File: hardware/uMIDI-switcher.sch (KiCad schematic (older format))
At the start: 26 parts, among them U1 MC7809CD, U2 MC7809CD, U3 MC7809CD, U4 MC7809CD, X1 CONN_01X02, X14 uMIDI GPIO, X16 uMIDI Power, X2 CONN_01X02, X3 CONN_01X02, X4 CONN_01X02, X5 Jack_Stacked, X6 Jack_Stacked

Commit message: Re-Annotate
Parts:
- renumbered C9 to C10, C28 to C12, C10 to C8, C8 to C9, X14 to X6, X16 to X7, X6 to X8
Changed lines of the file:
@@
 $EndComp
 $Comp
-L C C9
+L C C10
 U 1 1 55B6FB17
 P 5900 5300
-F 0 "C9" H 5950 5400 50  0000 L CNN
+F 0 "C10" H 5950 5400 50  0000 L CNN
 F 1 "100n" H 5950 5200 50  0000 L CNN
 F 2 "Capacitors_SMD:C_0603" H 5938 5150 30  0001 C CNN
@@
 $EndComp
 $Comp
-L C C8
+L C C9
 U 1 1 55B708C3
 P 4900 5300
-F 0 "C8" H 4950 5400 50  0000 L CNN
+F 0 "C9" H 4950 5400 50  0000 L CNN
 F 1 "100n" H 4950 5200 50  0000 L CNN
 F 2 "Capacitors_SMD:C_0603" H 4938 5150 30  0001 C CNN
@@
 	3850 5500 3850 5450
 $Comp
-L CONN_01X10 X14
+L CONN_01X10 X6
 U 1 1 55FDA32A
 P 4350 1950
-F 0 "X14" H 4350 2500 50  0000 C CNN
+F 0 "X6" H 4350 2500 50  0000 C CNN
 F 1 "uMIDI GPIO" V 4450 1950 50  0000 C CNN
 F 2 "Connect:VASCH5x2" H 4350 1950 60  0001 C CNN
@@
 $EndComp
 $Comp
-L CONN_01X02 X16
+L CONN_01X02 X7
 U 1 1 55FDF236
 P 7550 5250
-F 0 "X16" H 7550 5400 50  0000 C CNN
+F 0 "X7" H 7550 5400 50  0000 C CNN
 F 1 "uMIDI Power" V 7650 5250 50  0000 C CNN
 F 2 "Connect:PINHEAD1-2" H 7550 5250 60  0001 C CNN
@@
 	7350 5050 7350 5200
 $Comp
-L C C28
+L C C12
 U 1 1 55FDFE71
 P 7100 5300
-F 0 "C28" H 6900 5400 50  0000 L CNN
+F 0 "C12" H 6900 5400 50  0000 L CNN
 F 1 "100n" H 6850 5200 50  0000 L CNN
 F 2 "Capacitors_SMD:C_0603" H 7138 5150 30  0001 C CNN
@@
 	7350 5500 7350 5300
 $Comp
-L C C10
+L C C8
 U 1 1 55FECDD5
 P 4550 5300
-F 0 "C10" H 4600 5400 50  0000 L CNN
+F 0 "C8" H 4600 5400 50  0000 L CNN
 F 1 "10u" H 4600 5200 50  0000 L CNN
 F 2 "Capacitors_SMD:C_1206" H 4588 5150 30  0001 C CNN
@@
 Connection ~ 1550 2000
 $Comp
-L Jack_Stacked X6
+L Jack_Stacked X8
 U 1 1 56223ACE
 P 8300 2650
-F 0 "X6" H 7450 4650 60  0000 C CNN
+F 0 "X8" H 7450 4650 60  0000 C CNN
 F 1 "Jack_Stacked" H 7400 2900 60  0000 C CNN
 F 2 "uMIDI-switcher:NSJ12HF-1" H 8300 2650 60  0001 C CNN

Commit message: Change LDO supplier
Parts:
- U1, U2, U3, U4: Manufacturer (none) -> ON Semiconductor; Manufacturer Part Number (none) -> MC7809CD2TG; Part Number MC7809CD2TGOS-ND -> 863-MC7809CD2TG; Supplier Digikey -> Mouser
- X5, X8: Manufacturer (none) -> Neutrik; Manufacturer Part Number (none) -> NSJ12HF-1

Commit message: Add some component fields; Change 10uF footprint
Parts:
- C1, C10, C12, C2, C3, C4, C5, C6, C9: Manufacturer (none) -> Murata; Manufacturer Part Number (none) -> GRM188R71E104KA01D; Supplier Link (none) -> http://eu.mouser.com/ProductDetail/Murata-Electronics/GRM18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; Supplier Part Number (none) -> 81-GRM39X104K25
- C11, C7, C8: footprint Capacitors_SMD:C_1206 -> Capacitors_SMD:C_0805; Manufacturer (none) -> Murata; Manufacturer Link (none) -> http://psearch.en.murata.com/capacitor/lineup/grm/; Manufacturer Part Number (none) -> GRM21BR61E106KA73L; Supplier Link (none) -> http://eu.mouser.com/ProductDetail/Murata-Electronics/GRM21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; Supplier Part Number (none) -> 81-GRM21BR61E106KA3L
- D1: Part Number 621-B160-F -> (none); Supplier Link (none) -> http://eu.mouser.com/ProductDetail/Diodes-Incorporated/B160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; Supplier Part Number (none) -> 621-B160-F
- R1: Manufacturer (none) -> Vishay/Dale; Manufacturer Link (none) -> http://www.vishay.com/resistors-fixed/list/product-20011/; Manufacturer Part Number (none) -> CRCW0603100MJPEAHR; Supplier Link (none) -> http://eu.mouser.com/ProductDetail/Vishay-Dale/CRCW0603100M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; Supplier Part Number (none) -> 71-CRCW0603100MJPEA
- U1, U2, U3, U4: Part Number 863-MC7809CD2TG -> (none); Supplier Link (none) -> http://eu.mouser.com/ProductDetail/ON-Semiconductor/MC7809C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; Supplier Part Number (none) -> 863-MC7809CD2TG
- X5, X8: Part Number 568-NSJ12HF-1 -> (none); Supplier Link (none) -> http://www.mouser.de/ProductDetail/Neutrik/NSJ12HF-1/?qs=%2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; Supplier Part Number (none) -> 568-NSJ12HF-1
- X6: Manufacturer (none) -> 3M Electronic Solutions Division; Manufacturer Link (none) -> 30310-6002HB; Supplier Link (none) -> http://eu.mouser.com/ProductDetail/3M-Electronic-Solutions-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; Supplier Part Number (none) -> 517-30310-6002

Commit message: Fix ribbon connector supplier fields
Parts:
- X6: Manufacturer Link 30310-6002HB -> (none); Manufacturer Part Number (none) -> 30310-6002HB
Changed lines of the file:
@@
 F 6 "http://eu.mouser.com/ProductDetail/3M-Electronic-Solutions-Division/30310-6002HB/?qs=sGAEpiMZZMs%252bGHln7q6pmwu5ra4CY41iHF1AQhwXwqM%3d" H 4350 2500 60  0001 C CNN "Supplier Link"
 F 7 "3M Electronic Solutions Division" H 4350 2500 60  0001 C CNN "Manufacturer"
-F 8 "" H 4350 2500 60  0001 C CNN "Manufacturer Part Number"
-F 9 "30310-6002HB" H 4350 2500 60  0001 C CNN "Manufacturer Link"
+F 8 "30310-6002HB" H 4350 2500 60  0001 C CNN "Manufacturer Part Number"
 	1    4350 1950
 	-1   0    0    -1

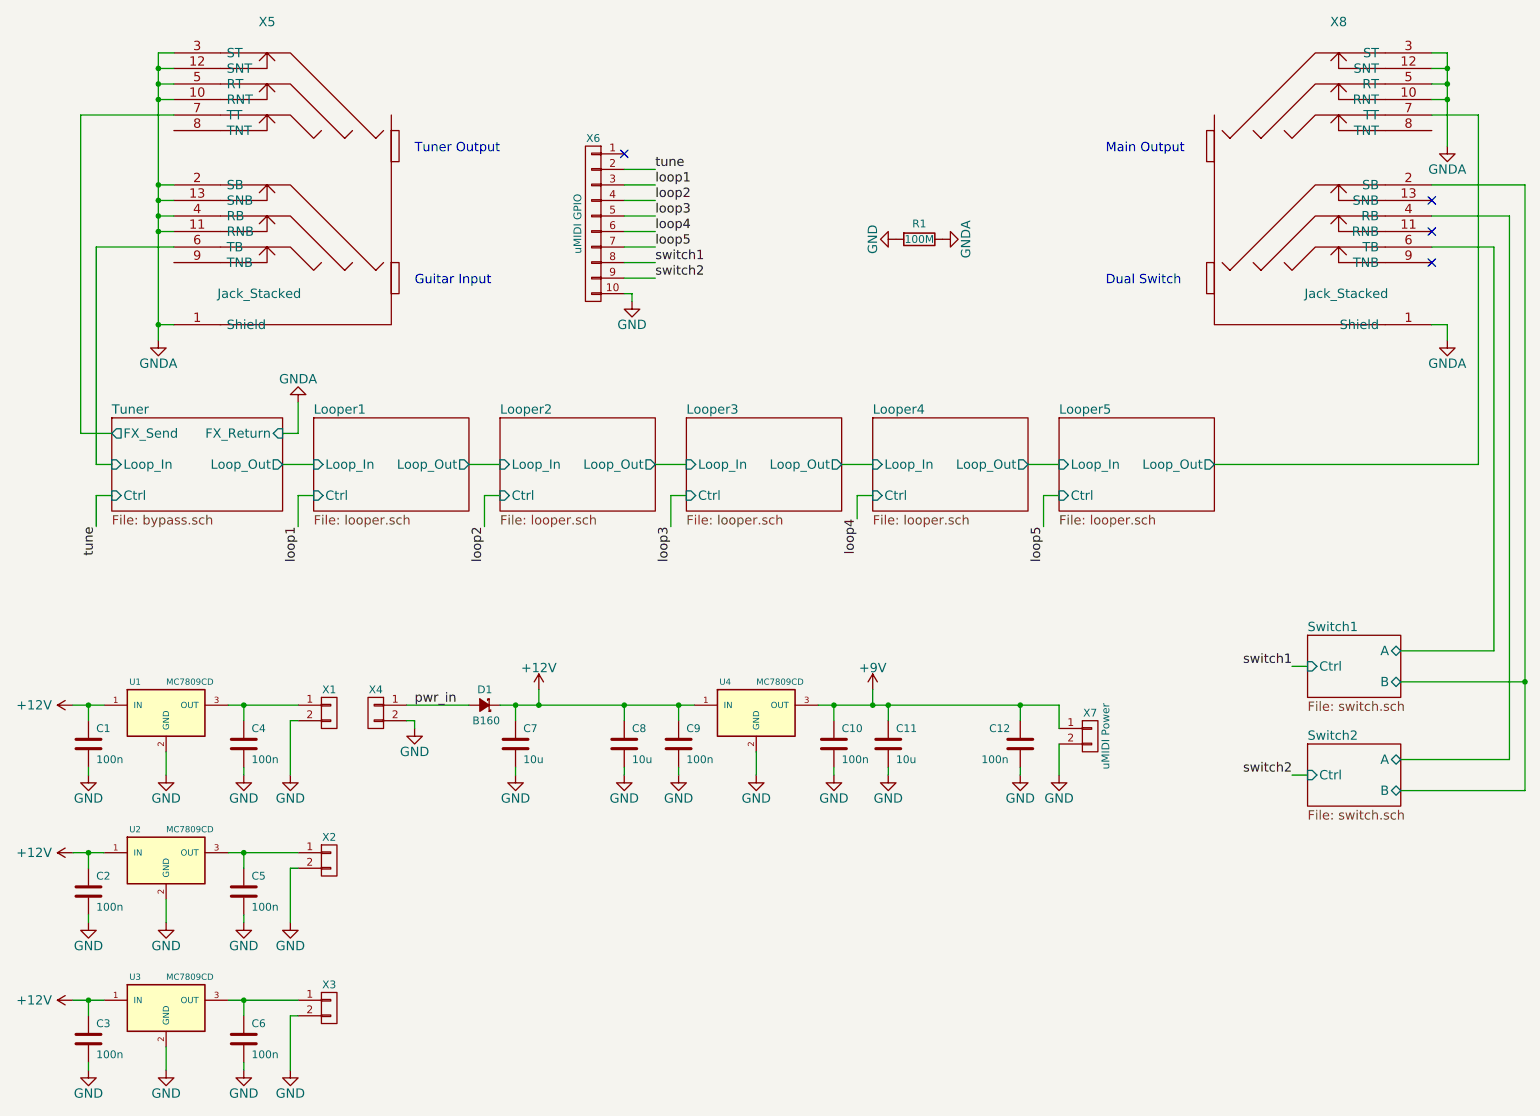
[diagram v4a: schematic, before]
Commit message: Straighten annotation and placement
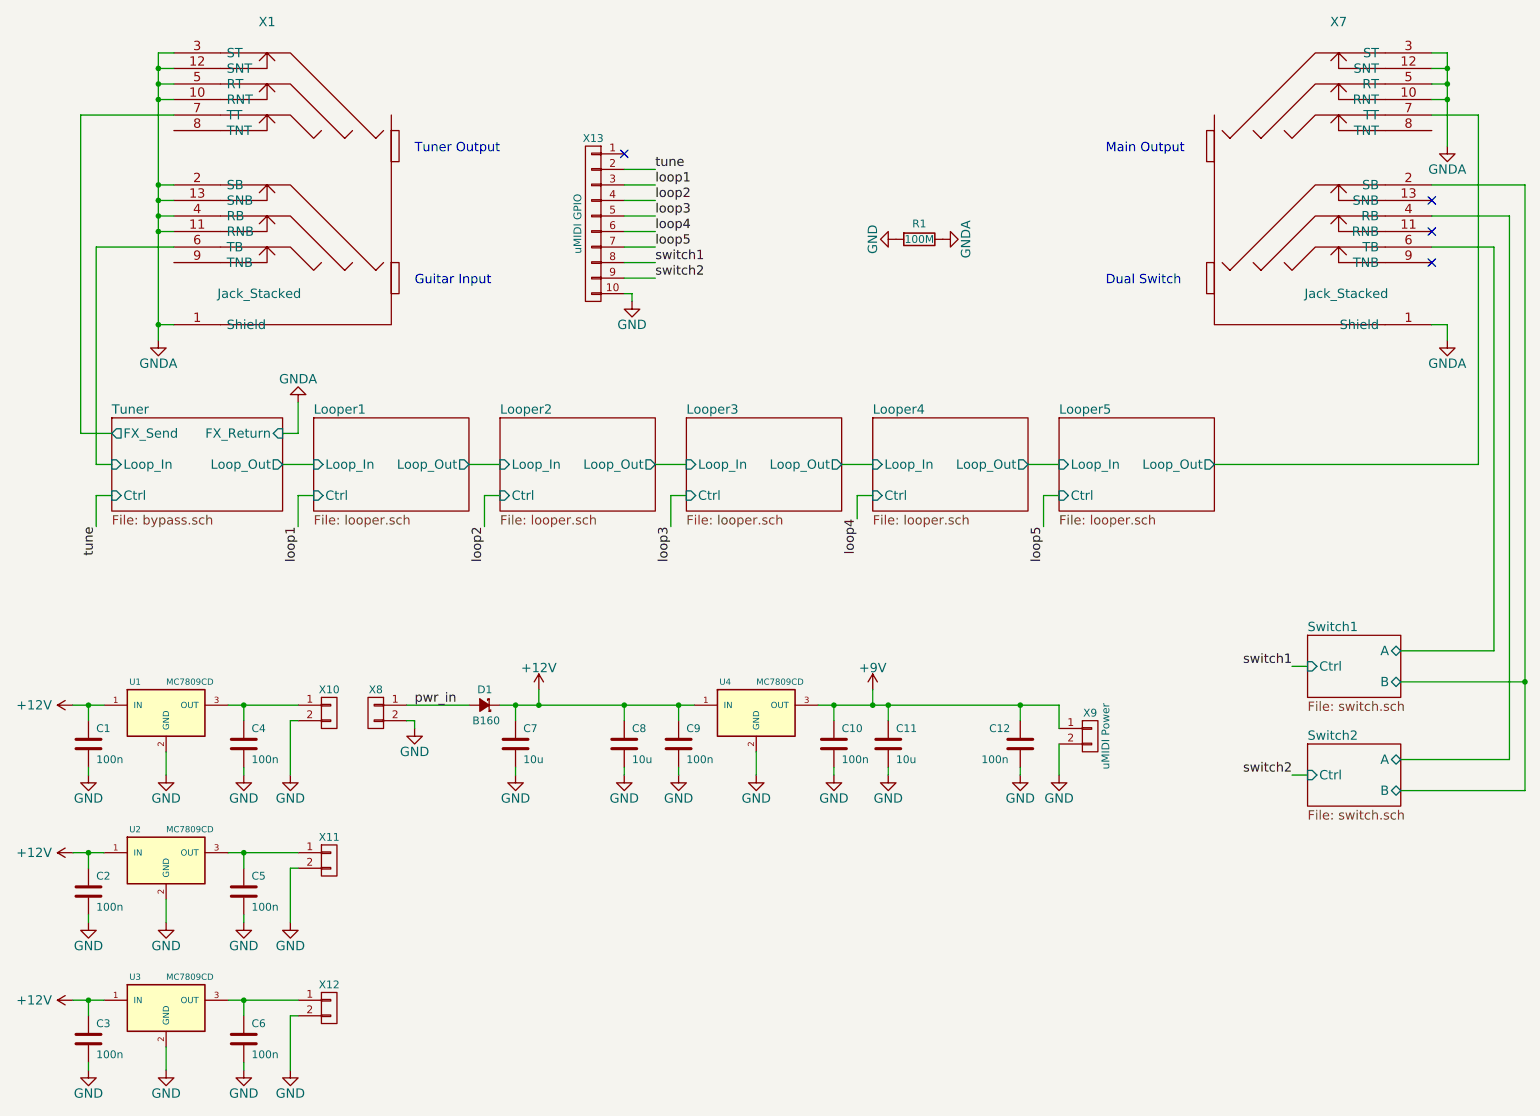
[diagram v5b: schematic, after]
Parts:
- X8: renamed from X4; value CONN_01X02 -> 12V in
- renumbered X5 to X1, X1 to X10, X2 to X11, X3 to X12, X6 to X13, X8 to X7, X7 to X9
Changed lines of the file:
@@
 $EndComp
 $Comp
-L CONN_01X02 X1
+L CONN_01X02 X10
 U 1 1 55B757F4
 P 2650 5100
-F 0 "X1" H 2650 5250 50  0000 C CNN
+F 0 "X10" H 2650 5250 50  0000 C CNN
 F 1 "CONN_01X02" V 2750 5100 50  0001 C CNN
 F 2 "Connect:PINHEAD1-2" H 2650 5100 60  0001 C CNN
 F 3 "" H 2650 5100 60  0000 C CNN
 F 4 "Mouser" H 3650 5050 60  0001 C CNN "Supplier"
-F 5 "" H 3650 5050 60  0001 C CNN "Part Number"
-F 6 "" H 3650 5050 60  0001 C CNN "Manufacturer"
-F 7 "" H 3650 5050 60  0001 C CNN "Manufacturer Part Number"
 	1    2650 5100
 	1    0    0    -1
@@
 $EndComp
 $Comp
-L CONN_01X02 X4
+L CONN_01X02 X8
 U 1 1 55B76CFF
 P 2950 5100
-F 0 "X4" H 2950 5250 50  0000 C CNN
-F 1 "CONN_01X02" V 3050 5100 50  0001 C CNN
+F 0 "X8" H 2950 5250 50  0000 C CNN
+F 1 "12V in" V 3050 5100 50  0001 C CNN
 F 2 "Connect:PINHEAD1-2" H 2950 5100 60  0001 C CNN
 F 3 "" H 2950 5100 60  0000 C CNN
 F 4 "Mouser" H 3650 5050 60  0001 C CNN "Supplier"
-F 5 "" H 3650 5050 60  0001 C CNN "Part Number"
-F 6 "" H 3650 5050 60  0001 C CNN "Manufacturer"
-F 7 "" H 3650 5050 60  0001 C CNN "Manufacturer Part Number"
 	1    2950 5100
 	-1   0    0    -1
@@
 $EndComp
 $Comp
-L CONN_01X02 X2
+L CONN_01X02 X11
 U 1 1 55F436A4
 P 2650 6050
-F 0 "X2" H 2650 6200 50  0000 C CNN
+F 0 "X11" H 2650 6200 50  0000 C CNN
 F 1 "CONN_01X02" V 2750 6050 50  0001 C CNN
 F 2 "Connect:PINHEAD1-2" H 2650 6050 60  0001 C CNN
 F 3 "" H 2650 6050 60  0000 C CNN
 F 4 "Mouser" H 3650 5050 60  0001 C CNN "Supplier"
-F 5 "" H 3650 5050 60  0001 C CNN "Part Number"
-F 6 "" H 3650 5050 60  0001 C CNN "Manufacturer"
-F 7 "" H 3650 5050 60  0001 C CNN "Manufacturer Part Number"
 	1    2650 6050
 	1    0    0    -1
@@
 $EndComp
 $Comp
-L CONN_01X02 X3
+L CONN_01X02 X12
 U 1 1 55F437D1
 P 2650 7000
-F 0 "X3" H 2650 7150 50  0000 C CNN
+F 0 "X12" H 2650 7150 50  0000 C CNN
 F 1 "CONN_01X02" V 2750 7000 50  0001 C CNN
 F 2 "Connect:PINHEAD1-2" H 2650 7000 60  0001 C CNN
 F 3 "" H 2650 7000 60  0000 C CNN
 F 4 "Mouser" H 3650 5050 60  0001 C CNN "Supplier"
-F 5 "" H 3650 5050 60  0001 C CNN "Part Number"
-F 6 "" H 3650 5050 60  0001 C CNN "Manufacturer"
-F 7 "" H 3650 5050 60  0001 C CNN "Manufacturer Part Number"
 	1    2650 7000
 	1    0    0    -1
@@
 	3850 5500 3850 5450
 $Comp
-L CONN_01X10 X6
+L CONN_01X10 X13
 U 1 1 55FDA32A
 P 4350 1950
-F 0 "X6" H 4350 2500 50  0000 C CNN
+F 0 "X13" H 4350 2500 50  0000 C CNN
 F 1 "uMIDI GPIO" V 4450 1950 50  0000 C CNN
 F 2 "Connect:VASCH5x2" H 4350 1950 60  0001 C CNN
@@
 $EndComp
 $Comp
-L CONN_01X02 X7
+L CONN_01X02 X9
 U 1 1 55FDF236
 P 7550 5250
-F 0 "X7" H 7550 5400 50  0000 C CNN
+F 0 "X9" H 7550 5400 50  0000 C CNN
 F 1 "uMIDI Power" V 7650 5250 50  0000 C CNN
 F 2 "Connect:PINHEAD1-2" H 7550 5250 60  0001 C CNN
 F 3 "" H 7550 5250 60  0000 C CNN
 F 4 "Mouser" H 3650 5050 60  0001 C CNN "Supplier"
-F 5 "" H 3650 5050 60  0001 C CNN "Part Number"
-F 6 "" H 3650 5050 60  0001 C CNN "Manufacturer"
-F 7 "" H 3650 5050 60  0001 C CNN "Manufacturer Part Number"
 	1    7550 5250
 	1    0    0    -1
@@
 $EndSheet
 $Comp
-L Jack_Stacked X5
+L Jack_Stacked X1
 U 1 1 56223AA2
 P 3100 2650
-F 0 "X5" H 2250 4650 60  0000 C CNN
+F 0 "X1" H 2250 4650 60  0000 C CNN
 F 1 "Jack_Stacked" H 2200 2900 60  0000 C CNN
 F 2 "uMIDI-switcher:NSJ12HF-1" H 3100 2650 60  0001 C CNN
@@
 Connection ~ 1550 2000
 $Comp
-L Jack_Stacked X8
+L Jack_Stacked X7
 U 1 1 56223ACE
 P 8300 2650
-F 0 "X8" H 7450 4650 60  0000 C CNN
+F 0 "X7" H 7450 4650 60  0000 C CNN
 F 1 "Jack_Stacked" H 7400 2900 60  0000 C CNN
 F 2 "uMIDI-switcher:NSJ12HF-1" H 8300 2650 60  0001 C CNN

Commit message: Use new ldo footprint; Adapt placement
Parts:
- U1, U2, U3, U4: footprint TO_SOT_Packages_SMD:TO-252-2Lead -> uMIDI-switcher:D2PAK-3
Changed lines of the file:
@@
 F 0 "U1" H 1400 5300 40  0000 C CNN
 F 1 "MC7809CD" H 1600 5300 40  0000 L CNN
-F 2 "TO_SOT_Packages_SMD:TO-252-2Lead" H 1600 5300 30  0001 C CIN
+F 2 "uMIDI-switcher:D2PAK-3" H 1600 5300 30  0001 C CIN
 F 3 "http://www.onsemi.com/pub_link/Collateral/MC7800-D.PDF" H 1400 5300 60  0001 C CNN
 F 4 "Mouser" H 1400 5300 60  0001 C CNN "Supplier"
@@
 F 0 "U2" H 1400 6250 40  0000 C CNN
 F 1 "MC7809CD" H 1600 6250 40  0000 L CNN
-F 2 "TO_SOT_Packages_SMD:TO-252-2Lead" H 1600 6250 30  0001 C CIN
+F 2 "uMIDI-switcher:D2PAK-3" H 1600 6250 30  0001 C CIN
 F 3 "http://www.onsemi.com/pub_link/Collateral/MC7800-D.PDF" H 1400 6250 60  0001 C CNN
 F 4 "Mouser" H 1400 6250 60  0001 C CNN "Supplier"
@@
 F 0 "U3" H 1400 7200 40  0000 C CNN
 F 1 "MC7809CD" H 1600 7200 40  0000 L CNN
-F 2 "TO_SOT_Packages_SMD:TO-252-2Lead" H 1600 7200 30  0001 C CIN
+F 2 "uMIDI-switcher:D2PAK-3" H 1600 7200 30  0001 C CIN
 F 3 "http://www.onsemi.com/pub_link/Collateral/MC7800-D.PDF" H 1400 7200 60  0001 C CNN
 F 4 "Mouser" H 1400 7200 60  0001 C CNN "Supplier"
@@
 F 0 "U4" H 5200 5300 40  0000 C CNN
 F 1 "MC7809CD" H 5400 5300 40  0000 L CNN
-F 2 "TO_SOT_Packages_SMD:TO-252-2Lead" H 5400 5300 30  0001 C CIN
+F 2 "uMIDI-switcher:D2PAK-3" H 5400 5300 30  0001 C CIN
 F 3 "http://www.onsemi.com/pub_link/Collateral/MC7800-D.PDF" H 5200 5300 60  0001 C CNN
 F 4 "Mouser" H 5200 5300 60  0001 C CNN "Supplier"

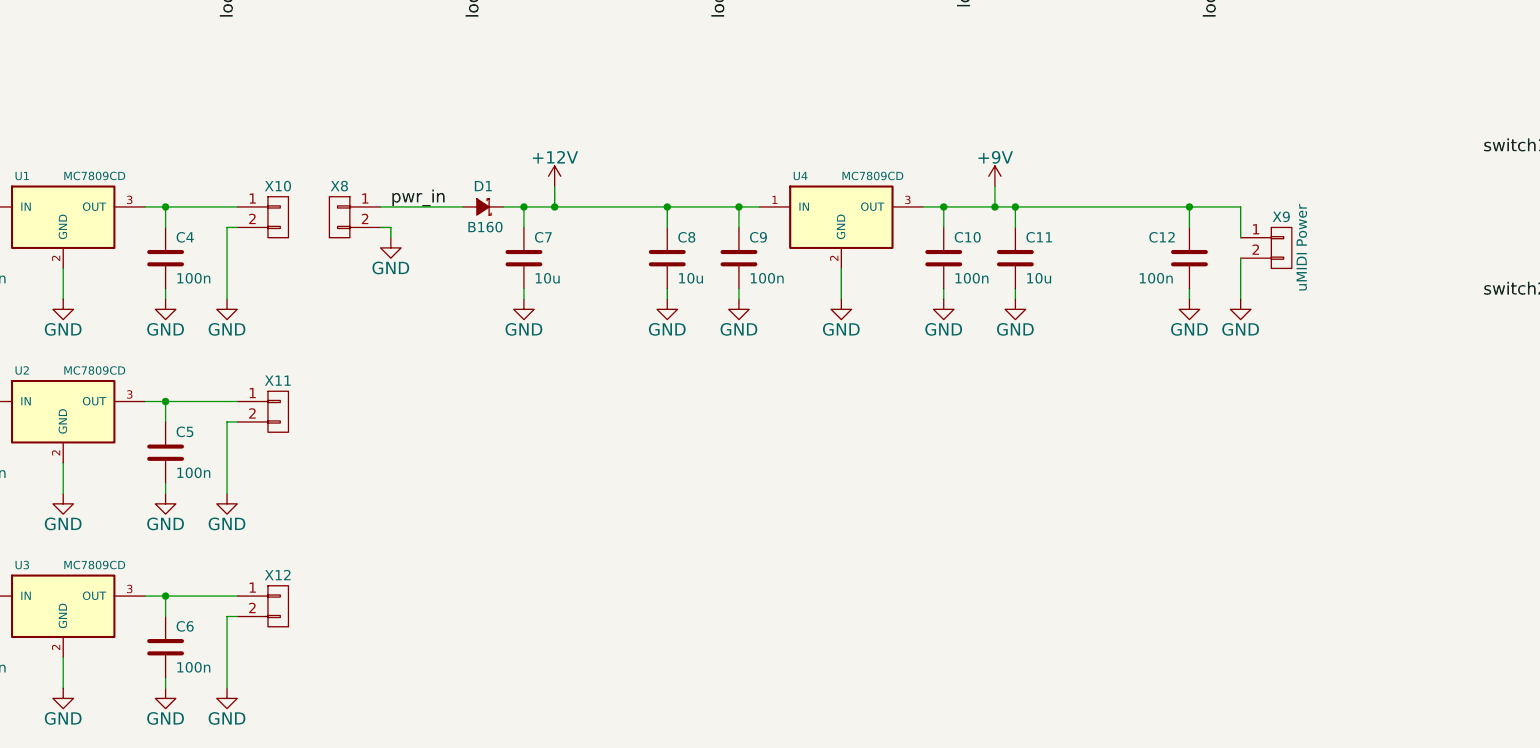
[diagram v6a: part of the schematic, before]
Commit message: Add 10uF caps to 9V outputs; Place and route
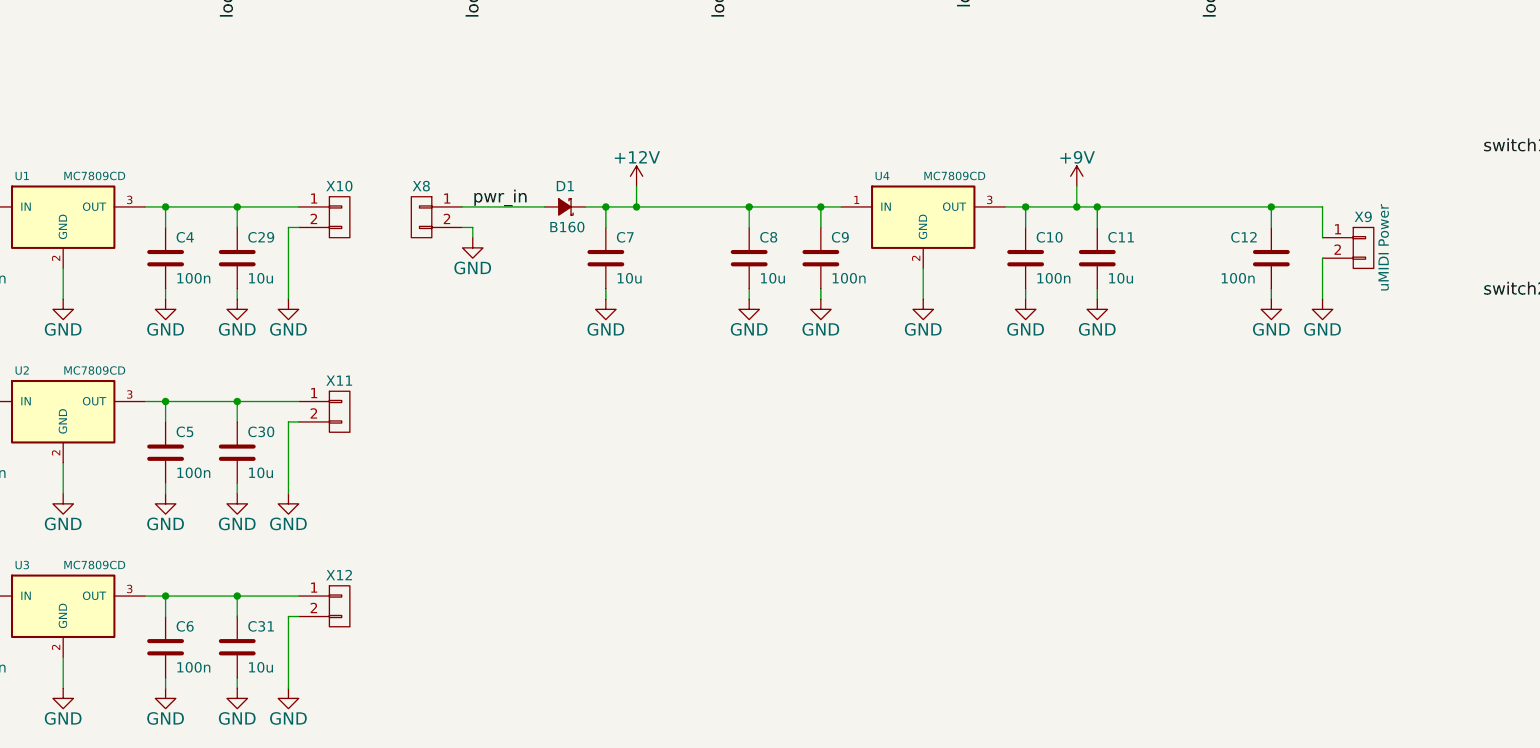
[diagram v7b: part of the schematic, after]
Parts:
- added C29, C30, C31: 10u, Capacitors_SMD:C_0805, symbol C
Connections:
- net GND: now also C29.2, C30.2, C31.2
- net at C4.1, U1.3 (OUT), X10.1 (P1): now also C29.1
- net at C5.1, U2.3 (OUT), X11.1 (P1): now also C30.1
- net at C6.1, U3.3 (OUT), X12.1 (P1): now also C31.1
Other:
- moved on the sheet: C10, C11, C12, C7, C8, C9, D1, U4, X10, X11, X12, X8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
